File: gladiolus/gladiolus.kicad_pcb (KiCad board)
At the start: 4 copper layers, 70.7 x 53.3 mm, 133 parts, among them J1 NEIGHBOR1, J2 NEIGHBOR2, J7 BONUS_ROW, P1 CONN_01X05, Q1 Q_NPN_BEC, U1 THS4520RGT, U2 AD8330ARQZ, U3 AD9283, U4 AD9704, U5 LMH6643

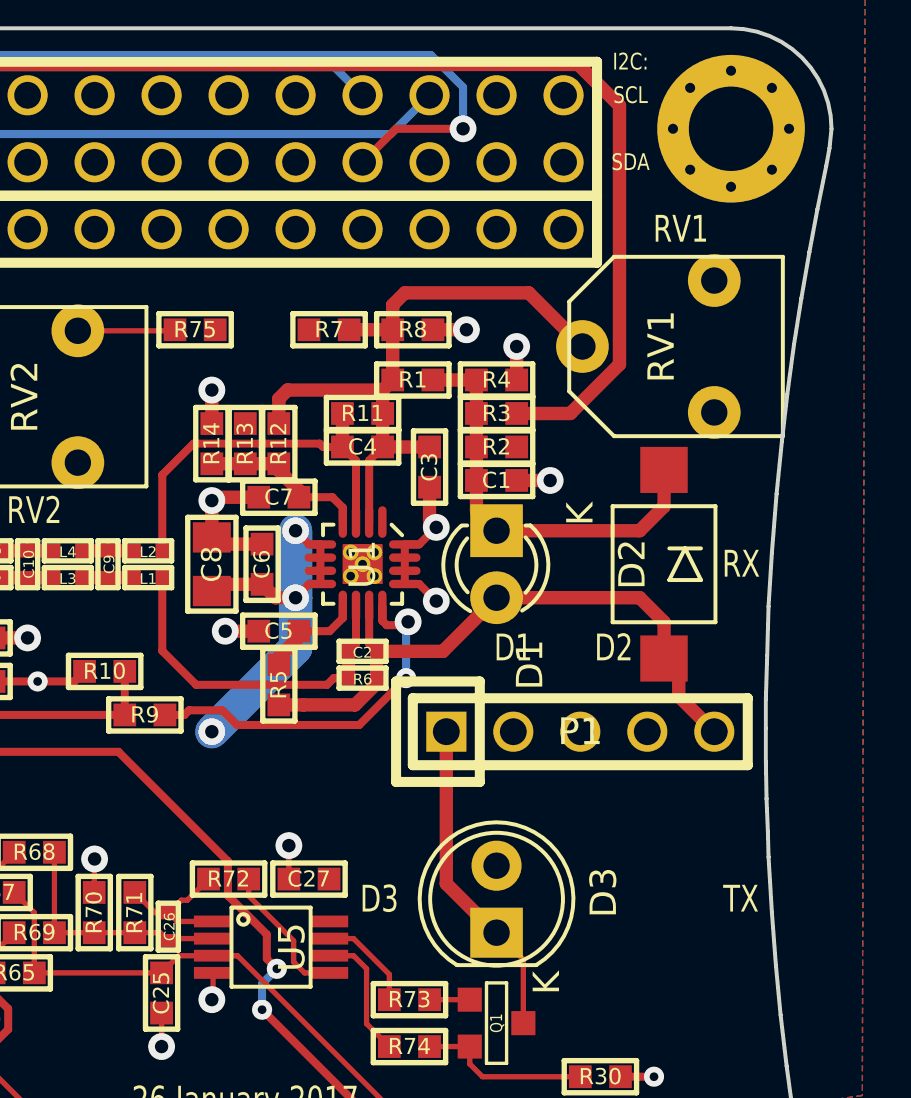
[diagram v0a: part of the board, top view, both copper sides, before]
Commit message: Added AC/DC coupling switch and removed central header
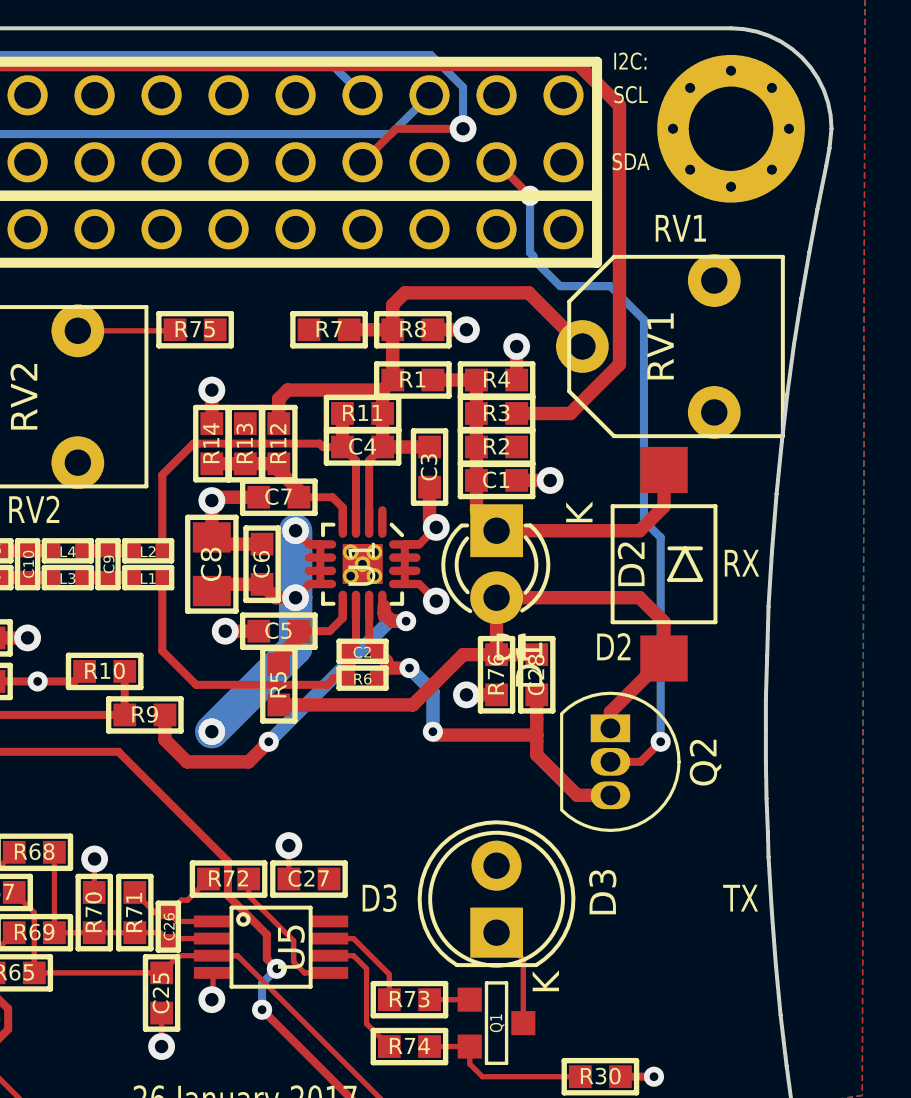
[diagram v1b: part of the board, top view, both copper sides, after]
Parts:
- removed P1: CONN_01X05, gsg-modules:HEADER-1x5
- added C28: 8nF, gsg-modules:0603, F.Cu at (169.2, 93.1)
- added Q2: BS, Package_TO_SOT_THT:TO-92_Inline, F.Cu at (172.0, 95.1)
- added R76: 1M, gsg-modules:0603, F.Cu at (167.6, 93.1)
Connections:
- C2 pad 2: /RXIN -> Net-(C2-Pad2)
- R6 pad 2: /RXIN -> Net-(C2-Pad2)
- U1 pad 11: /RXIN -> Net-(C2-Pad2)
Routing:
- net /P3_5: track 0.00 -> 27.9 mm, vias 0 -> 2
- net Net-(C2-Pad2): track 0.00 -> 16.5 mm, vias 0 -> 2
- net /TXOUT: track 12.3 -> 3.85 mm
- net GND: track 78.3 -> 79.4 mm, vias 39 -> 40
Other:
- board text added: "mount either RX or TX diode on reverse side"

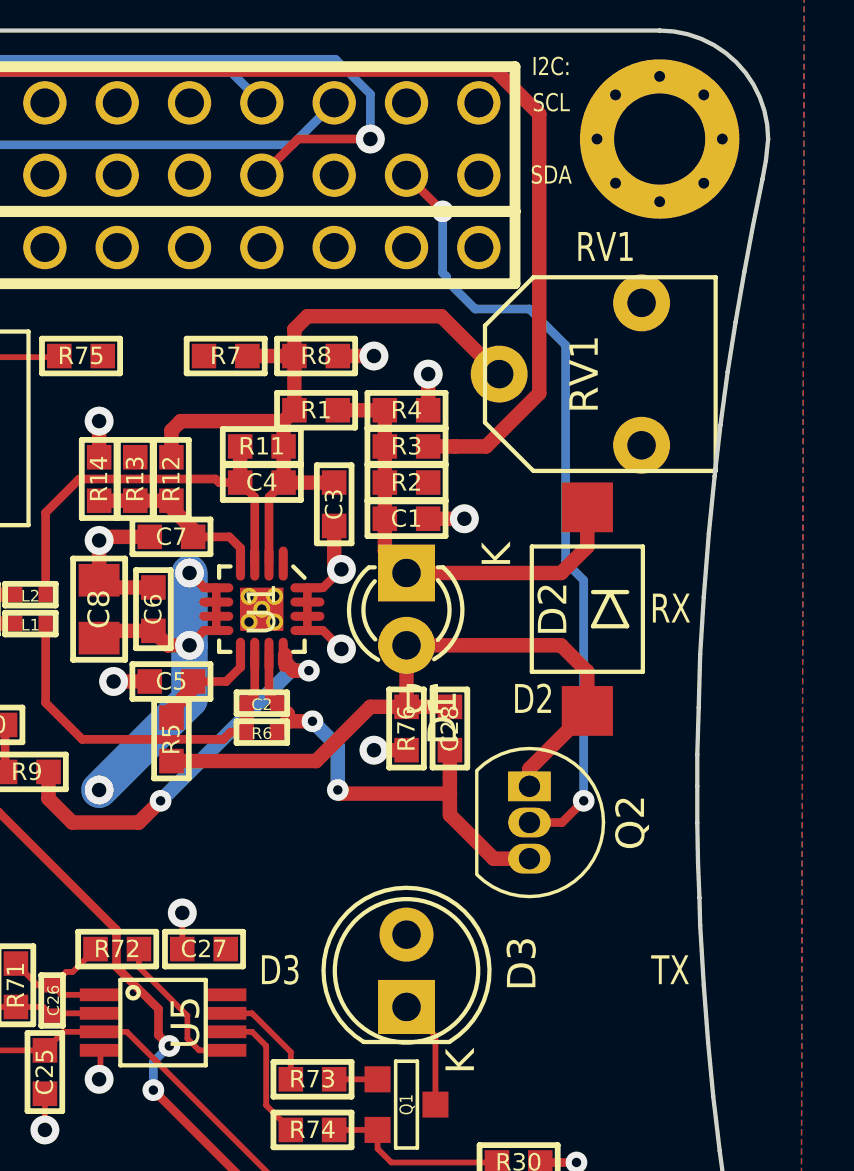
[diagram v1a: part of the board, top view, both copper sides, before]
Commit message: Added AC/DC coupling switch using 74LVC1G3157
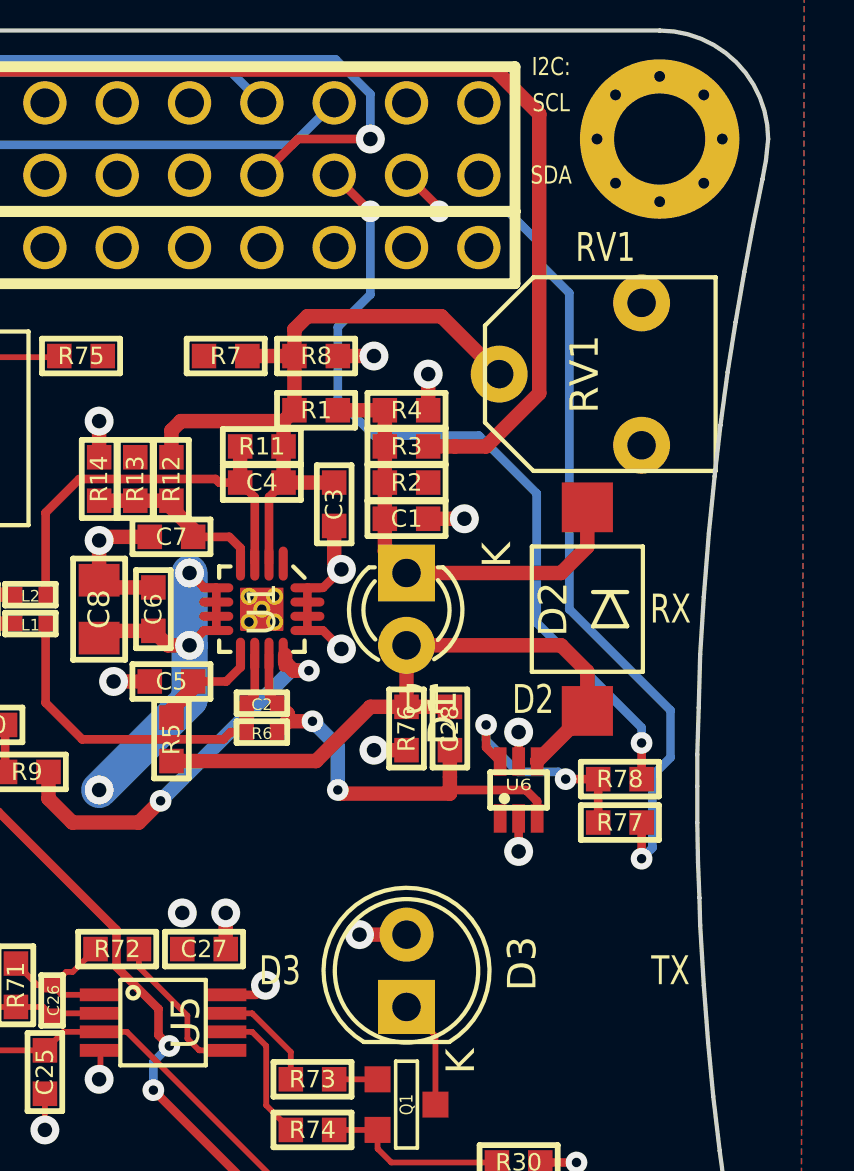
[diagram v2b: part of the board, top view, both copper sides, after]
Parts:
- removed Q2: BS, Package_TO_SOT_THT:TO-92_Inline
- added R77: 0, gsg-modules:0603, F.Cu at (175.1, 96.4)
- added R78: 0, gsg-modules:0603, F.Cu at (175.1, 94.9)
- added U6: 74LVC1G3157, gsg-modules:SOT363, F.Cu at (171.6, 95.2)
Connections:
- J1 pad 10: /P1_1 -> (no net)
- J1 pad 11: /CLK0 -> (no net)
- J1 pad 12: /P1_2 -> (no net)
- J1 pad 24: /P5_4 -> (no net)
- J1 pad 29: /P5_7 -> (no net)
- J1 pad 3: /P4_9 -> (no net)
- J1 pad 31: /P1_18 -> (no net)
- J1 pad 32: /P1_17 -> (no net)
- J1 pad 33: /P9_5 -> (no net)
- J1 pad 35: /P2_0 -> (no net)
- J1 pad 36: /P6_0 -> (no net)
- J1 pad 37: /P1_20 -> (no net)
- J1 pad 38: /P1_19 -> (no net)
- J1 pad 39: /P1_4 -> (no net)
- J1 pad 40: /P1_3 -> (no net)
- J1 pad 5: /P4_10 -> (no net)
- J1 pad 9: /P5_1 -> (no net)
- J2 pad 10: /P4_6 -> (no net)
- J2 pad 11: /P4_7 -> (no net)
- J2 pad 12: /CLK2 -> (no net)
- J2 pad 13: /P2_8 -> (no net)
- J2 pad 14: /P2_7 -> (no net)
- J2 pad 15: /P2_6 -> (no net)
- J2 pad 16: /P7_7 -> (no net)
- J2 pad 17: /WAKEUP0 -> (no net)
- J2 pad 19: /P2_4 -> (no net)
- J2 pad 21: /PF_4 -> (no net)
- J2 pad 22: /P3_2 -> (no net)
- J2 pad 23: /P7_2 -> (no net)
- J2 pad 24: /P3_1 -> (no net)
- J2 pad 25: /P7_1 -> (no net)
- J2 pad 26: /P3_0 -> (no net)
- J2 pad 27: /P7_0 -> (no net)
- J2 pad 28: /P3_4 -> (no net)
- J2 pad 29: /P6_8 -> (no net)
- J2 pad 30: /P3_7 -> (no net)
- J2 pad 31: /P6_7 -> (no net)
- J2 pad 32: /P3_3 -> (no net)
- J2 pad 38: /P3_6 -> (no net)
- J2 pad 39: /I2C0_SDA -> (no net)
- J2 pad 4: /P4_0 -> (no net)
- J2 pad 40: /I2C0_SCL -> (no net)
- J2 pad 6: /P4_5 -> (no net)
- J2 pad 8: /P4_2 -> (no net)
- J7 pad 11: /RESET -> (no net)
- J7 pad 12: /VBAT -> (no net)
- J7 pad 13: /P2_11 -> (no net)
- J7 pad 14: /P2_10 -> (no net)
- J7 pad 15: /P6_10 -> (no net)
- J7 pad 16: /P6_9 -> (no net)
- J7 pad 17: /P6_2 -> (no net)
- J7 pad 18: /P6_1 -> (no net)
- J7 pad 2: /P6_4 -> (no net)
- J7 pad 20: Net-(J7-Pad20) -> (no net)
- J7 pad 3: /P6_5 -> (no net)
- J7 pad 4: /ADC0_5 -> (no net)
- J7 pad 5: /ADC0_2 -> (no net)
- J7 pad 6: /P2_9 -> (no net)
- J7 pad 7: /P2_12 -> (no net)
- J7 pad 8: /P2_13 -> (no net)
- J7 pad 9: /RTC_ALARM -> (no net)
- U1 pad 1: Net-(U1-Pad1) -> (no net)
- U4 pad 13: Net-(U4-Pad13) -> (no net)
- U4 pad 4: Net-(U4-Pad4) -> (no net)
- U4 pad 5: Net-(U4-Pad5) -> (no net)
- U4 pad 6: Net-(U4-Pad6) -> (no net)
- U4 pad 7: Net-(U4-Pad7) -> (no net)
- U4 pad 8: Net-(U4-Pad8) -> (no net)
- U4 pad 9: Net-(U4-Pad9) -> (no net)
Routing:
- net /P2_1: track 0.00 -> 28.8 mm, vias 0 -> 2
- net Net-(R77-Pad1): track 0.00 -> 8.06 mm, vias 0 -> 2
- net VCC: track 109.5 -> 115.0 mm, vias 8 -> 12
- net /P3_5: track 27.9 -> 30.9 mm
- net /RXIN: track 24.3 -> 23.3 mm
- net GND: track 79.4 -> 79.3 mm, vias 40 -> 41

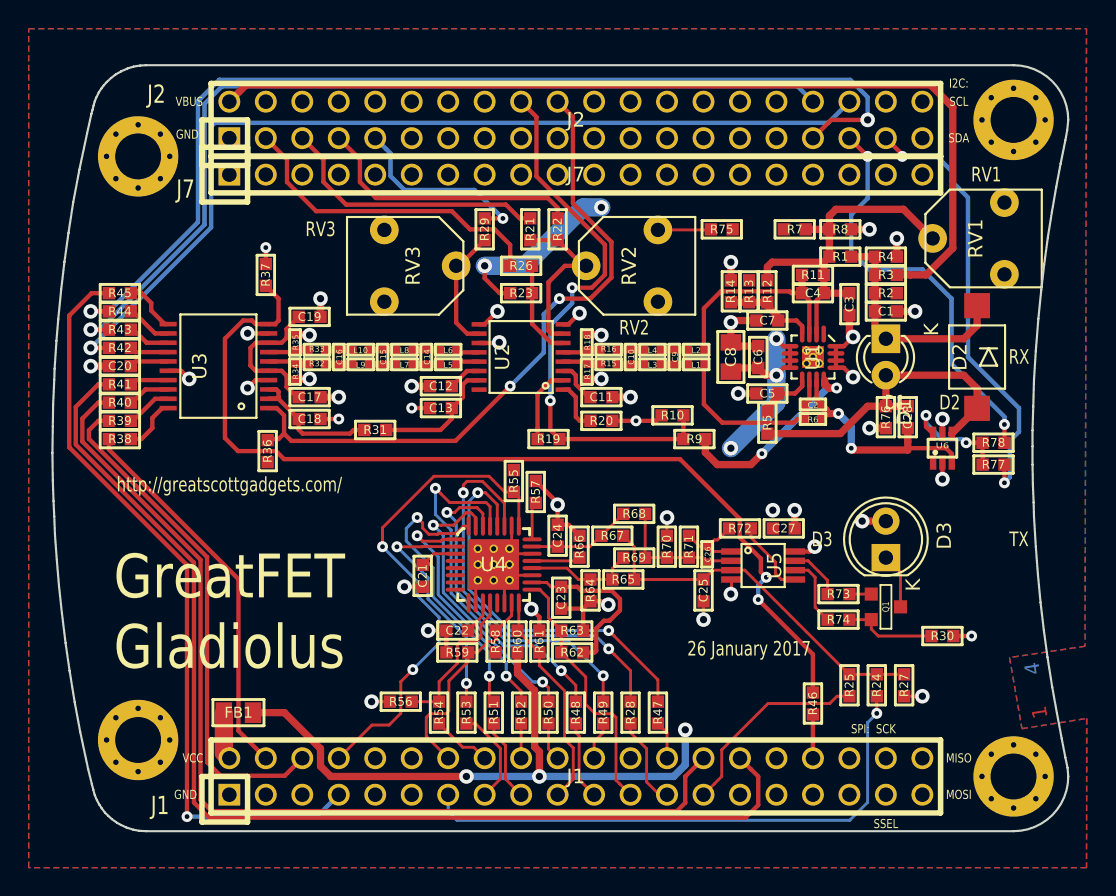
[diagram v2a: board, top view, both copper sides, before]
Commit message: Gladiolus: Added AD/DC coupling switch, removed DNP components for inversion, added switch to fully turn off TX, routed TX LED current to ADC
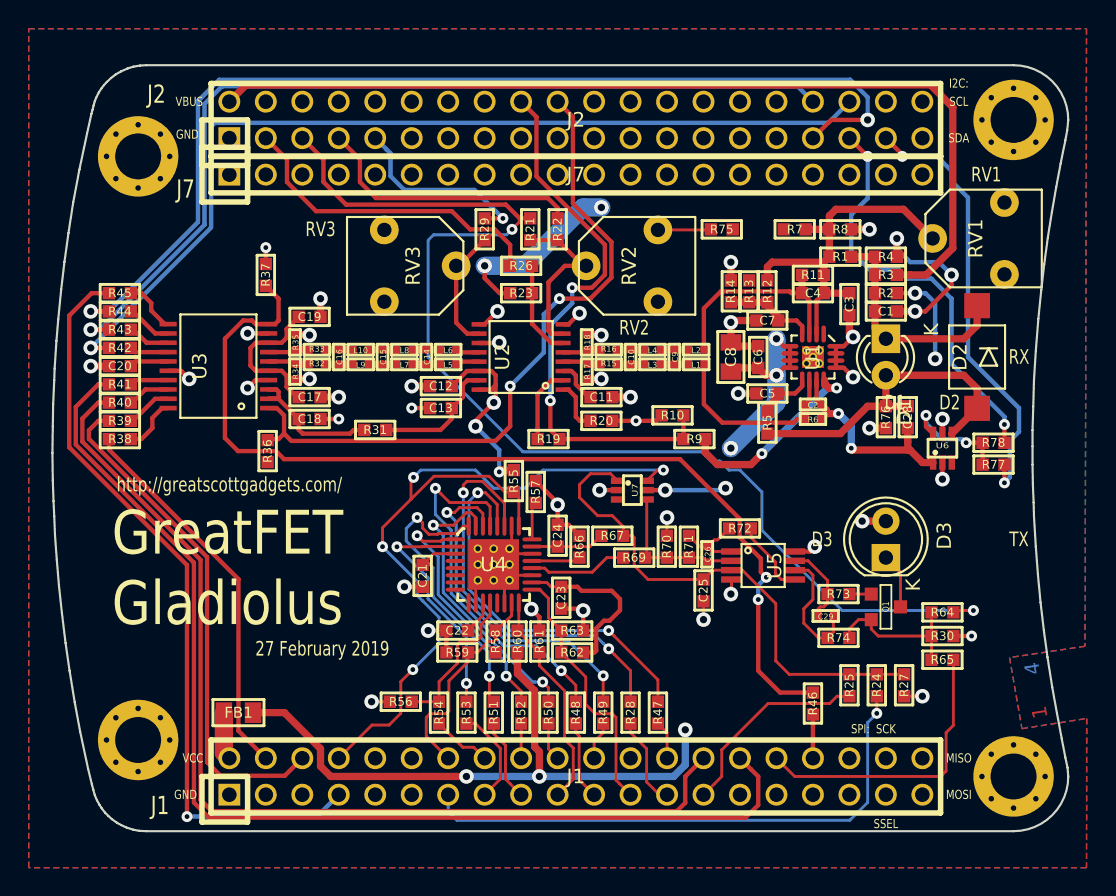
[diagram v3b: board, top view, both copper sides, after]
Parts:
- removed C27: 100nF, gsg-modules:0603
- removed R68: R, gsg-modules:0603
- added C29: 470pF, gsg-modules:0402, F.Cu at (163.4, 106.9)
- added U7: 74LVC1G3157, gsg-modules:SOT363, F.Cu at (150.0, 98.2)
- R64: value 249 -> 0
- R65: value R -> 0
- moved R64 24.6 mm to (171.6, 106.7), turned to 0 degrees
- moved R65 22.9 mm to (171.6, 110.0)
- moved R74 1.27 mm to (164.3, 108.5)
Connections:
- J1 pad 10: (no net) -> /P1_1
- J1 pad 11: (no net) -> /CLK0
- J1 pad 12: (no net) -> /P1_2
- J1 pad 24: (no net) -> /P5_4
- J1 pad 29: (no net) -> /P5_7
- J1 pad 3: (no net) -> /P4_9
- J1 pad 31: (no net) -> /P1_18
- J1 pad 32: (no net) -> /P1_17
- J1 pad 33: (no net) -> /P9_5
- J1 pad 35: (no net) -> /P2_0
- J1 pad 36: (no net) -> /P6_0
- J1 pad 37: (no net) -> /P1_20
- J1 pad 38: (no net) -> /P1_19
- J1 pad 39: (no net) -> /P1_4
- J1 pad 40: (no net) -> /P1_3
- J1 pad 5: (no net) -> /P4_10
- J1 pad 9: (no net) -> /P5_1
- J2 pad 10: (no net) -> /P4_6
- J2 pad 11: (no net) -> /P4_7
- J2 pad 12: (no net) -> /CLK2
- J2 pad 13: (no net) -> /P2_8
- J2 pad 14: (no net) -> /P2_7
- J2 pad 15: (no net) -> /P2_6
- J2 pad 16: (no net) -> /P7_7
- J2 pad 17: (no net) -> /WAKEUP0
- J2 pad 19: (no net) -> /P2_4
- J2 pad 21: (no net) -> /PF_4
- J2 pad 22: (no net) -> /P3_2
- J2 pad 23: (no net) -> /P7_2
- J2 pad 24: (no net) -> /P3_1
- J2 pad 25: (no net) -> /P7_1
- J2 pad 26: (no net) -> /P3_0
- J2 pad 27: (no net) -> /P7_0
- J2 pad 28: (no net) -> /P3_4
- J2 pad 29: (no net) -> /P6_8
- J2 pad 30: (no net) -> /P3_7
- J2 pad 31: (no net) -> /P6_7
- J2 pad 32: (no net) -> /P3_3
- J2 pad 38: (no net) -> /P3_6
- J2 pad 39: (no net) -> /I2C0_SDA
- J2 pad 4: (no net) -> /P4_0
- J2 pad 40: (no net) -> /I2C0_SCL
- J2 pad 6: (no net) -> /P4_5
- J2 pad 8: (no net) -> /P4_2
- J7 pad 11: (no net) -> /RESET
- J7 pad 12: (no net) -> /VBAT
- J7 pad 13: (no net) -> /P2_11
- J7 pad 14: (no net) -> /P2_10
- J7 pad 15: (no net) -> /P6_10
- J7 pad 16: (no net) -> /P6_9
- J7 pad 17: (no net) -> /P6_2
- J7 pad 18: (no net) -> /P6_1
- J7 pad 2: (no net) -> /P6_4
- J7 pad 20: (no net) -> Net-(J7-Pad20)
- J7 pad 3: (no net) -> /P6_5
- J7 pad 4: (no net) -> /ADC0_5
- J7 pad 5: (no net) -> /ADC0_2
- J7 pad 6: (no net) -> /P2_9
- J7 pad 7: (no net) -> /P2_12
- J7 pad 8: (no net) -> /P2_13
- J7 pad 9: (no net) -> /RTC_ALARM
- R64 pad 1: Net-(R64-Pad1) -> Net-(Q1-Pad2)
- R64 pad 2: GND -> /ADC0_0
- R65 pad 1: Net-(R64-Pad1) -> Net-(Q1-Pad2)
- R65 pad 2: Net-(C25-Pad1) -> /P1_17
- R69 pad 2: Net-(R64-Pad1) -> Net-(R69-Pad2)
- U1 pad 1: (no net) -> Net-(U1-Pad1)
- U4 pad 13: (no net) -> Net-(U4-Pad13)
- U4 pad 20: Net-(R64-Pad1) -> Net-(R69-Pad2)
- U4 pad 4: (no net) -> Net-(U4-Pad4)
- U4 pad 5: (no net) -> Net-(U4-Pad5)
- U4 pad 6: (no net) -> Net-(U4-Pad6)
- U4 pad 7: (no net) -> Net-(U4-Pad7)
- U4 pad 8: (no net) -> Net-(U4-Pad8)
- U4 pad 9: (no net) -> Net-(U4-Pad9)
- U6 pad 1: (no net) -> Net-(C2-Pad2)
- U6 pad 3: Net-(C2-Pad2) -> Net-(U6-Pad3)
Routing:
- net /ADC0_0: track 19.1 -> 83.9 mm, vias 0 -> 2
- net VCC: track 115.0 -> 137.7 mm, vias 12 -> 18
- net /P5_0: track 34.9 -> 56.6 mm, vias 2 -> 4
- net /P1_17: track 0.00 -> 20.5 mm
- net Net-(C25-Pad1): track 25.4 -> 36.2 mm
- net GND: track 79.3 -> 88.0 mm, vias 41 -> 42
- net Net-(R64-Pad1): track 7.76 -> 0.00 mm
- net Net-(R69-Pad2): track 0.00 -> 6.89 mm
- net Net-(Q1-Pad2): track 6.58 -> 10.8 mm
- net Net-(C29-Pad2): track 4.93 -> 8.79 mm
- net Net-(C24-Pad2): track 7.30 -> 5.14 mm
- net Net-(C29-Pad1): track 3.81 -> 5.75 mm
- net Net-(C2-Pad2): track 16.2 -> 14.4 mm
- net /P2_3: track 46.9 -> 48.6 mm
- net /ADCCLK: track 67.1 -> 68.4 mm
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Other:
- board text added: "27 February 2019"
- board text removed: "26 January 2017"
